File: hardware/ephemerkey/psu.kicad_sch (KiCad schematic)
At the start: 0 parts

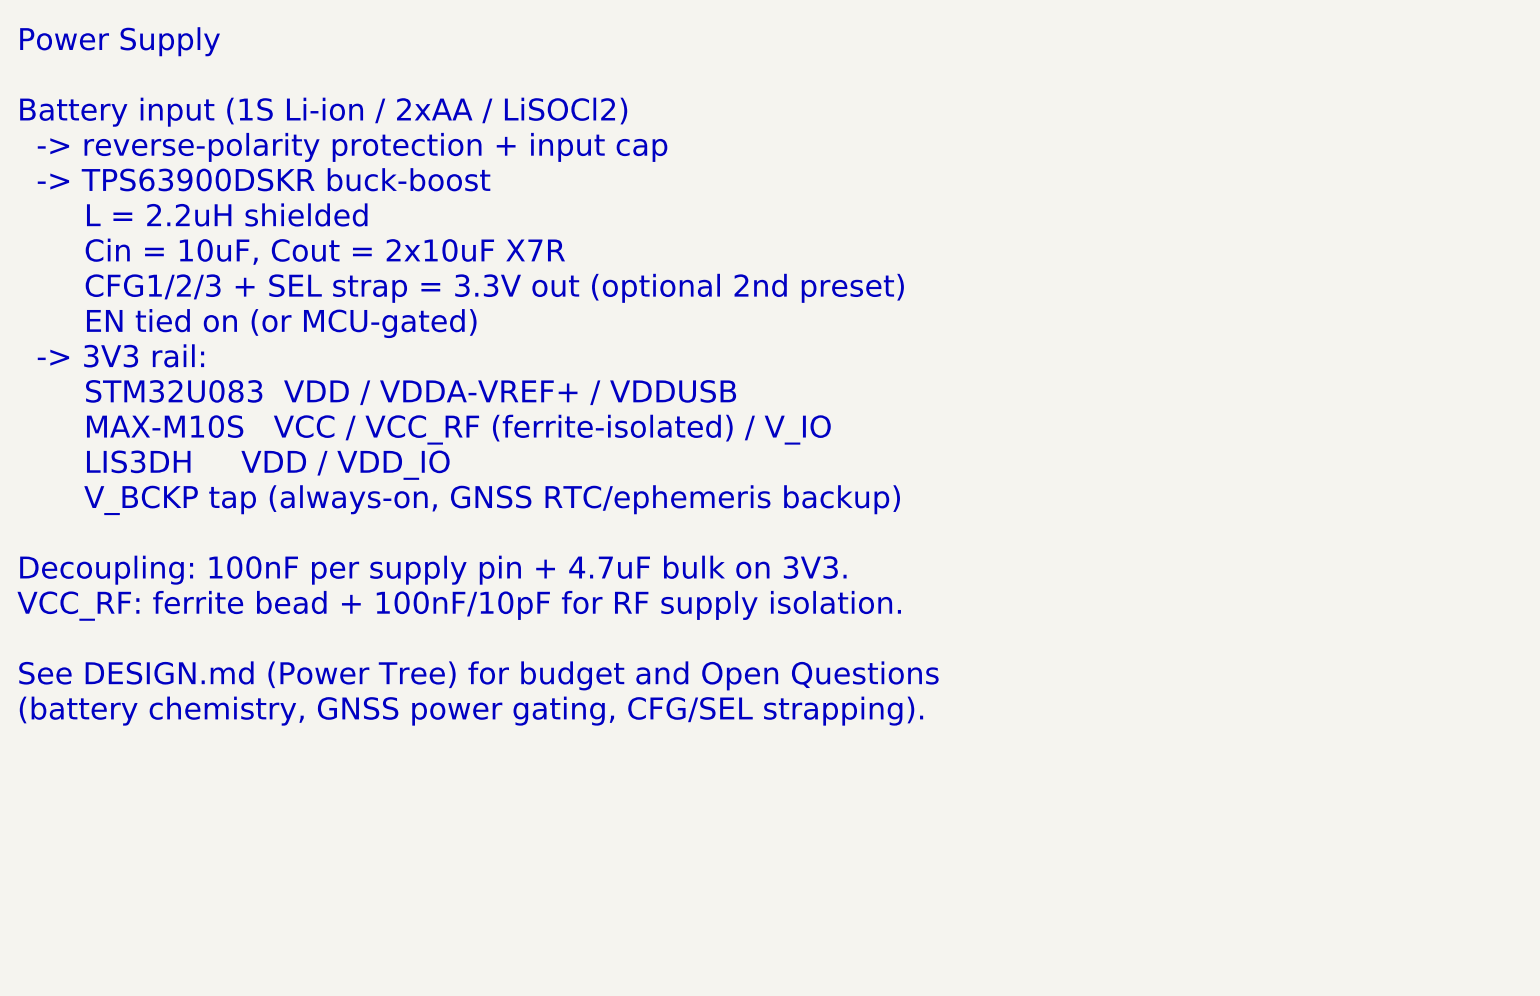
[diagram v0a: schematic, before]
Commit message: Add USB-C input + Li-ion charging subsystem (house parts)
Resolved power decisions: 1S Li-ion (rechargeable), USB-C powers+charges+
provisions, GNSS kept hot via V_BCKP. Charger/USB front-end reuses parts
already used in sibling projects for BOM consolidation:

- USB-C: GCT USB4105 (USB-TYPE-C-019, C2927039) — house-standard connector
- ESD:   USBLC6-2SC6 (C2687116)
- Charger: MCP73831T-2ACI/OT (C424093), Rprog sets Ichg
- Power path: AO3401A P-FET (C15127) load-share — run/charge from USB without
  cycling the battery; SYS feeds TPS63900 VIN (VBUS~4.7V or BAT 3.0-4.2V)

DESIGN.md: new power-tree, "USB-C input + Li-ion charging" section, parts +
library-map rows, resolved decisions/open-questions. PSU sheet annotation
updated to match.

Co-Authored-By: Claude Opus 4.8 (1M context) <noreply@anthropic.com>
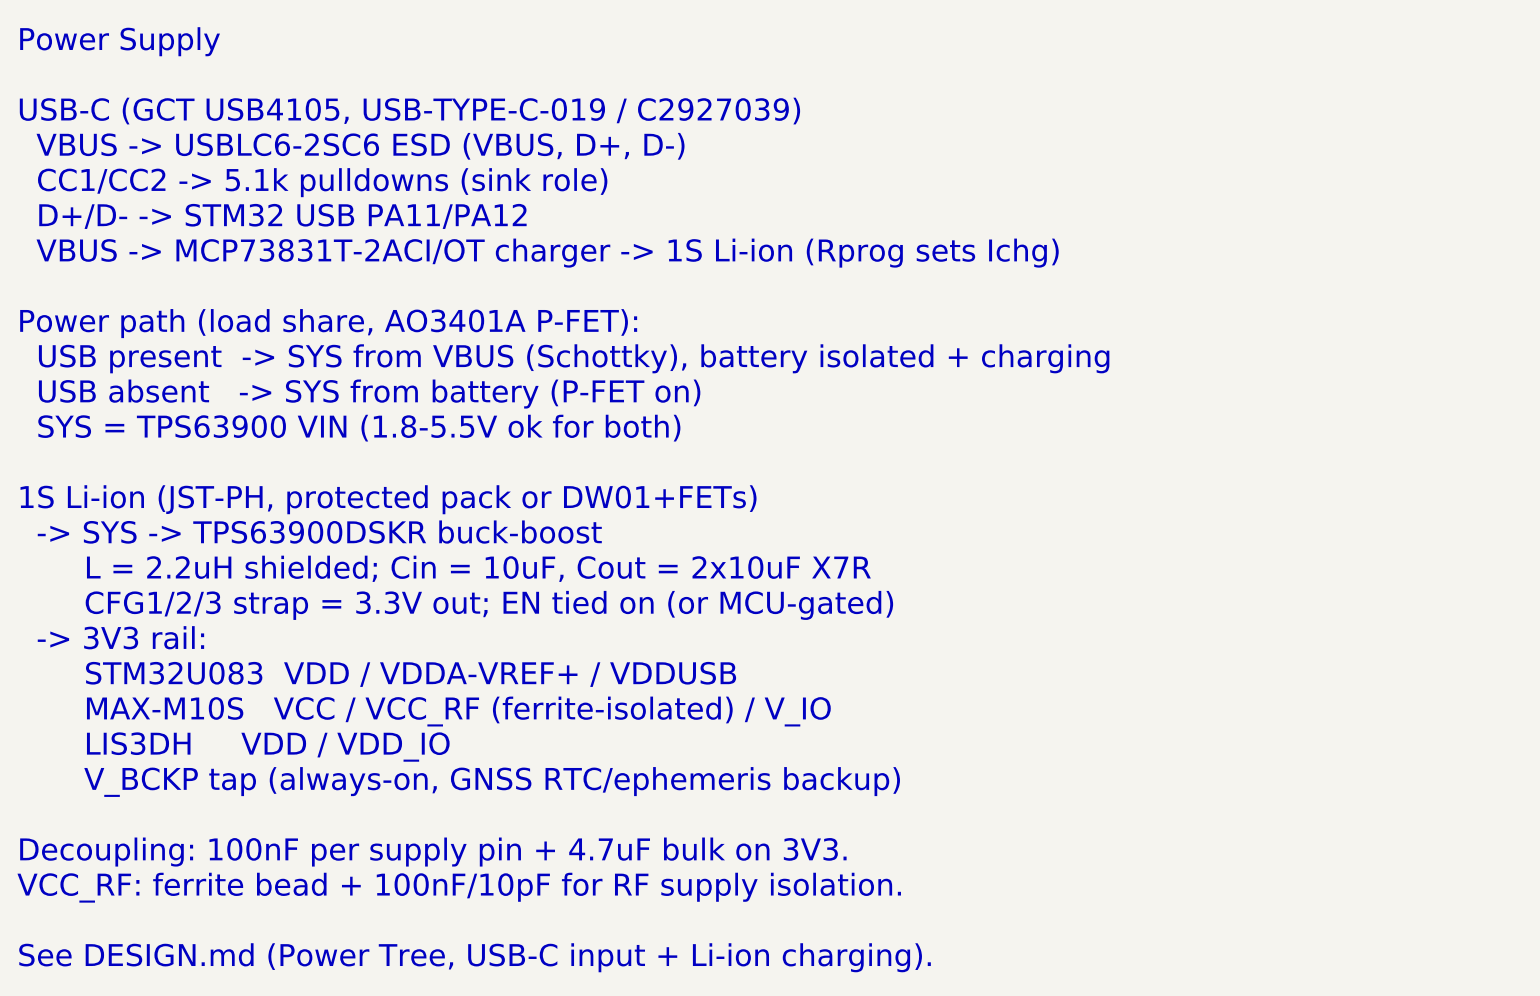
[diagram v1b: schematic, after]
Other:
- note added: "Power Supply USB-C (GCT USB4105, USB-TYPE-C-019 / C2927039) VBUS -> USBLC6-2SC6 ESD (VBUS, D+, D-) CC1/CC2 -> 5.1k pulldowns (sink role) D+/D- -> STM32 USB PA11/PA12 VBUS -> MCP73831T-2ACI/OT charger -> 1S Li-ion (Rprog sets Ichg) Power path (load share, AO3401A P-FET): USB present -> SYS from VBUS (Schottky), battery isolated + charging USB absent -> SYS from battery (P-FET on) SYS = TPS63900 VI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"
- note removed: "Power Supply Battery input (1S Li-ion / 2xAA / LiSOCl2) -> reverse-polarity protection + input cap -> TPS63900DSKR buck-boost L = 2.2uH shielded Cin = 10uF, Cout = 2x10uF X7R CFG1/2/3 + SEL strap = 3.3V out (optional 2nd preset) EN tied on (or MCU-gated) -> 3V3 rail: STM32U083 VDD / VDDA-VREF+ / VDDUSB MAX-M10S VCC / VCC_RF (ferrite-isolated) / V_IO LIS3DH VDD / VDD_IO V_BCKP tap (always-on, GNSS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"
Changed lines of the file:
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@@
 		(comment 2 "Ultra-low Iq for long battery life")
 	)
-	(text "Power Supply\n\nBattery input (1S Li-ion / 2xAA / LiSOCl2)\n  -> reverse-polarity protection + input cap\n  -> TPS63900DSKR buck-boost\n       L = 2.2uH shielded\n       Cin = 10uF, Cout = 2x10uF X7R\n       CFG1/2/3 + SEL strap = 3.3V out (optional 2nd preset)\n       EN tied on (or MCU-gated)\n  -> 3V3 rail:\n       STM32U083  VDD / VDDA-VREF+ / VDDUSB\n       MAX-M10S   VCC / VCC_RF (ferrite-isolated) / V_IO\n       LIS3DH     VDD / VDD_IO\n       V_BCKP tap (always-on, GNSS RTC/ephemeris backup)\n\nDecoupling: 100nF per supply pin + 4.7uF bulk on 3V3.\nVCC_RF: ferrite bead + 100nF/10pF for RF supply isolation.\n\nSee DESIGN.md (Power Tree) for budget and Open Questions\n(battery chemistry, GNSS power gating, CFG/SEL strapping)."
+	(text "Power Supply\n\nUSB-C (GCT USB4105, USB-TYPE-C-019 / C2927039)\n  VBUS -> USBLC6-2SC6 ESD (VBUS, D+, D-)\n  CC1/CC2 -> 5.1k pulldowns (sink role)\n  D+/D- -> STM32 USB PA11/PA12\n  VBUS -> MCP73831T-2ACI/OT charger -> 1S Li-ion (Rprog sets Ichg)\n\nPower path (load share, AO3401A P-FET):\n  USB present  -> SYS from VBUS (Schottky), battery isolated + charging\n  USB absent   -> SYS from battery (P-FET on)\n  SYS = TPS63900 VIN (1.8-5.5V ok for both)\n\n1S Li-ion (JST-PH, protected pack or DW01+FETs)\n  -> SYS -> TPS63900DSKR buck-boost\n       L = 2.2uH shielded; Cin = 10uF, Cout = 2x10uF X7R\n       CFG1/2/3 strap = 3.3V out; EN tied on (or MCU-gated)\n  -> 3V3 rail:\n       STM32U083  VDD / VDDA-VREF+ / VDDUSB\n       MAX-M10S   VCC / VCC_RF (ferrite-isolated) / V_IO\n       LIS3DH     VDD / VDD_IO\n       V_BCKP tap (always-on, GNSS RTC/ephemeris backup)\n\nDecoupling: 100nF per supply pin + 4.7uF bulk on 3V3.\nVCC_RF: ferrite bead + 100nF/10pF for RF supply isolation.\n\nSee DESIGN.md (Power Tree, USB-C input + Li-ion charging)."
 		(exclude_from_sim no)
 		(at 25.4 25.4 0)

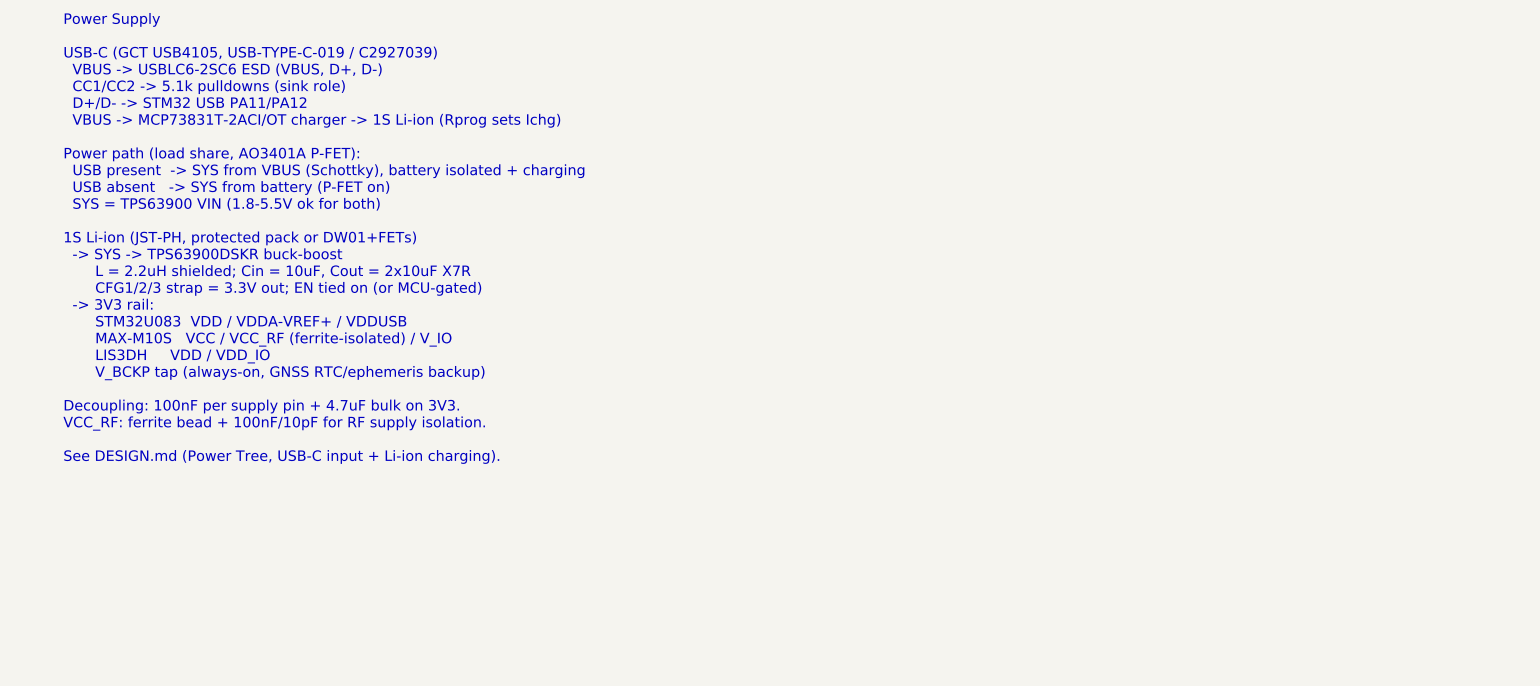
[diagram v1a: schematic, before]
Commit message: Populate schematic sheets per subsystem (placed, not wired)
Adopt the house schgen workflow (kschgen.py + manifest), matching notchdeck/
tsumikoro: schematic is GENERATED from scripts/ephemerkey.schgen.py, parts
PLACED with per-sheet on-canvas wiring notes; wiring is the next eeschema phase.

57 components across MCU / PSU / GNSS / Sensors, every line on a real KiCad
bundled symbol+footprint and a JLCPCB LCSC (0402 passives, 0805 bulk):
- MCU: STM32U083KCU6, 32.768kHz LSE crystal (C32346) + 12pF loads, SWD TC2030,
  lock-out header, decoupling, BOOT0/NRST, button, status LEDs.
- PSU: USB-C (GCT USB4105) + USBLC6 ESD + 5.1k CC, MCP73831 charger (Rprog 4.7k
  ~213mA for 500mAh), AO3401A load-share + B5819W, TPS63900 + FNR3015 2.2µH
  (small) + 10µF caps, JST-PH RA battery (S2B-PH-K-S).
- GNSS: MAX-M10S + W3011A + pi-match (series 0R, shunts DNP), VCC_RF ferrite,
  V_BCKP/V_IO/VCC decoupling.
- Sensors: LIS3DH + decoupling + 4.7k I2C pull-ups.

Tooling: kschgen.py, kicad-sch-check.py, kicad-sch-render.sh; Makefile gen/
check/render targets. make check: 57 comps, 57/57 footprints, no dup refs.
Added hardware/PARTS.md (BOM source of truth). CLAUDE.md documents the workflow.

Co-Authored-By: Claude Opus 4.8 (1M context) <noreply@anthropic.com>
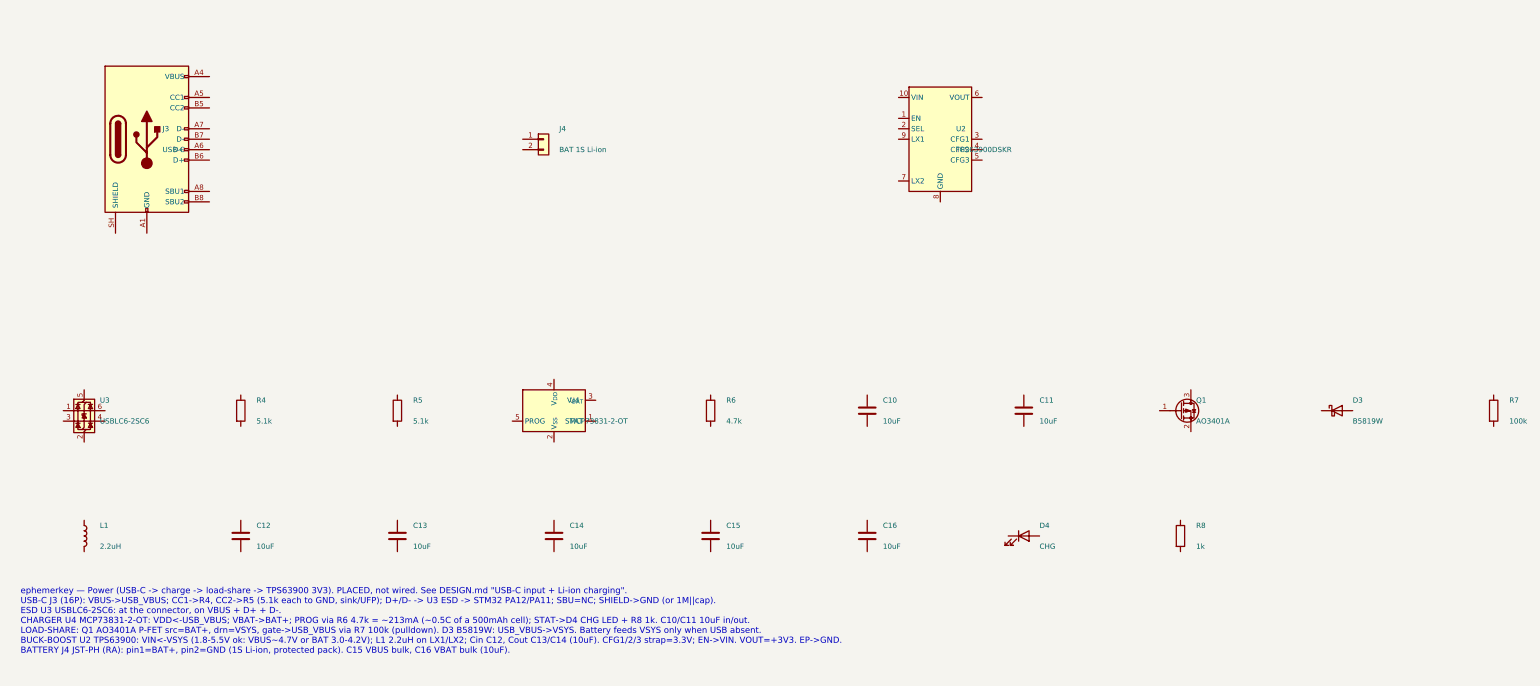
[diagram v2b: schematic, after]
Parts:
- added C10, C11, C12, C13, C14, C15, C16: 10uF, Capacitor_SMD:C_0805_2012Metric, symbol Device:C
- added D3: B5819W, Diode_SMD:D_SOD-123, symbol Device:D_Schottky
- added D4: CHG, LED_SMD:LED_0402_1005Metric, symbol Device:LED
- added J3: USB-C, Connector_USB:USB_C_Receptacle_GCT_USB4105-xx-A_16P_TopMnt_Horizontal, symbol Connector:USB_C_Receptacle_USB2.0_16P
- added J4: BAT 1S Li-ion, Connector_JST:JST_PH_S2B-PH-K_1x02_P2.00mm_Horizontal, symbol Connector_Generic:Conn_01x02
- added L1: 2.2uH, Inductor_SMD:L_Changjiang_FNR3015S, symbol Device:L
- added Q1: AO3401A, Package_TO_SOT_SMD:SOT-23, symbol Transistor_FET:Q_PMOS_GSD
- added R4, R5: 5.1k, Resistor_SMD:R_0402_1005Metric, symbol Device:R
- added R6: 4.7k, Resistor_SMD:R_0402_1005Metric, symbol Device:R
- added R7: 100k, Resistor_SMD:R_0402_1005Metric, symbol Device:R
- added R8: 1k, Resistor_SMD:R_0402_1005Metric, symbol Device:R
- added U2: TPS63900DSKR, Package_SON:WSON-10-1EP_2.5x2.5mm_P0.5mm_EP1.2x2mm, symbol Regulator_Switching:TPS63900
- added U3: USBLC6-2SC6, Package_TO_SOT_SMD:SOT-23-6, symbol Power_Protection:USBLC6-2SC6
- added U4: MCP73831-2-OT, Package_TO_SOT_SMD:SOT-23-5, symbol Battery_Management:MCP73831-2-OT
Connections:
- new net: U2.11 (GND), U2.8 (GND)
- new net: J3.A1 (GND), J3.A12 (GND), J3.B1 (GND), J3.B12 (GND)
- new net: J3.A4 (VBUS), J3.A9 (VBUS), J3.B4 (VBUS), J3.B9 (VBUS)
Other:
- note added: "ephemerkey — Power (USB-C -> charge -> load-share -> TPS63900 3V3). PLACED, not wired. See DESIGN.md "USB-C input + Li-ion charging". USB-C J3 (16P): VBUS->USB_VBUS; CC1->R4, CC2->R5 (5.1k each to GND, sink/UFP); D+/D- -> U3 ESD -> STM32 PA12/PA11; SBU=NC; SHIELD->GND (or 1M||cap). ESD U3 USBLC6-2SC6: at the connector, on VBUS + D+ + D-. CHARGER U4 MCP73831-2-OT: VDD<-USB_VBUS; VBAT->BAT+; PROG v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"
- note removed: "Power Supply USB-C (GCT USB4105, USB-TYPE-C-019 / C2927039) VBUS -> USBLC6-2SC6 ESD (VBUS, D+, D-) CC1/CC2 -> 5.1k pulldowns (sink role) D+/D- -> STM32 USB PA11/PA12 VBUS -> MCP73831T-2ACI/OT charger -> 1S Li-ion (Rprog sets Ichg) Power path (load share, AO3401A P-FET): USB present -> SYS from VBUS (Schottky), battery isolated + charging USB absent -> SYS from battery (P-FET on) SYS = TPS63900 VI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"
- company: (none) -> EphemerKey Authors
- title: ephemerkey — Power Supply -> ephemerkey — USB-C / Li-ion charge / load-share / buck-boost
